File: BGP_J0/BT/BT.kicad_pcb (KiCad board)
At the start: 2 copper layers, 28 x 25 mm, 21 parts, among them P1 CONN_01X02, P2 CONN_01X02, P3 CONN_01X02, P4 CONN_01X04, P5 CONN_01X02, Q1 J202

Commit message: PCB Layout cleanup
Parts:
- moved RV1 5.10 mm to (158.2, 88.1), turned to 0 degrees
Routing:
- net Net-(C3-Pad1): track 13.7 -> 7.61 mm
- net Net-(Q1-Pad2): track 18.4 -> 22.5 mm
- net VCC: track 14.4 -> 12.8 mm
- net /Vref: track 0.00 -> 1.36 mm
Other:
- rule trace_min: 0.2 -> 0.3
- rule via_min_size: 0.4 -> 0.6
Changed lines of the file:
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@@
     (links 34)
     (no_connects 0)
-    (area 132.924999 78.924999 161.075001 104.075001)
+    (area 130.364286 78.924999 161.175001 105.75588)
     (thickness 1.6)
     (drawings 8)
-    (tracks 104)
+    (tracks 106)
     (zones 0)
     (modules 21)
@@
     (zone_clearance 0.3)
     (zone_45_only no)
-    (trace_min 0.2)
+    (trace_min 0.3)
     (segment_width 0.2)
     (edge_width 0.15)
     (via_size 0.6)
     (via_drill 0.4)
-    (via_min_size 0.4)
+    (via_min_size 0.6)
     (via_min_drill 0.3)
     (uvia_size 0.3)
     (uvia_drill 0.1)
     (uvias_allowed no)
-    (uvia_min_size 0.2)
+    (uvia_min_size 0.3)
     (uvia_min_drill 0.1)
     (pcb_text_width 0.3)
@@
   )
   (module Potentiometers:Potentiometer_Trimmer_Bourns_3296W (layer B.Cu)
-    (at 153.1 88.1 180)
+    (at 158.2 88.1)
     (descr "Spindle Trimmer Potentiometer, Bourns 3296W, https://www.bourns.com/pdfs/3296.pdf")
     (tags "Spindle Trimmer Potentiometer   Bourns 3296W")
-    (fp_text reference RV1 (at 1.56 3 180) (layer B.SilkS)
+    (fp_text reference RV1 (at 1.56 3) (layer B.SilkS)
       (effects (font (size 0.6 0.6) (thickness 0.15)) (justify mirror))
     )
-    (fp_text value POT (at -2.54 -3.67 180) (layer B.Fab) hide
+    (fp_text value POT (at -2.54 -3.67) (layer B.Fab) hide
       (effects (font (size 0.6 0.6) (thickness 0.15)) (justify mirror))
     )
@@
     (fp_line (start 2.5 -2.7) (end 2.5 2.7) (layer B.CrtYd) (width 0.05))
     (fp_line (start 2.5 2.7) (end -7.6 2.7) (layer B.CrtYd) (width 0.05))
-    (pad 1 thru_hole circle (at 0 0 180) (size 1.44 1.44) (drill 0.8) (layers *.Cu *.Mask)
+    (pad 1 thru_hole circle (at 0 0) (size 1.44 1.44) (drill 0.8) (layers *.Cu *.Mask)
       (net 16 "Net-(Q1-Pad2)"))
-    (pad 2 thru_hole circle (at -2.54 0 180) (size 1.44 1.44) (drill 0.8) (layers *.Cu *.Mask)
+    (pad 2 thru_hole circle (at -2.54 0) (size 1.44 1.44) (drill 0.8) (layers *.Cu *.Mask)
       (net 16 "Net-(Q1-Pad2)"))
-    (pad 3 thru_hole circle (at -5.08 0 180) (size 1.44 1.44) (drill 0.8) (layers *.Cu *.Mask)
+    (pad 3 thru_hole circle (at -5.08 0) (size 1.44 1.44) (drill 0.8) (layers *.Cu *.Mask)
       (net 4 "Net-(C3-Pad1)"))
     (model Potentiometers.3dshapes/Potentiometer_Trimmer_Bourns_3296W.wrl
@@
   (segment (start 141.5 99.10051) (end 143.80051 96.8) (width 0.3) (layer F.Cu) (net 2))
   (segment (start 146 96.4) (end 146 95.17602) (width 0.3) (layer F.Cu) (net 2))
+  (via (at 142.963596 91.736404) (size 0.6) (drill 0.4) (layers F.Cu B.Cu) (net 3))
+  (segment (start 143 92.9) (end 143 91.772808) (width 0.3) (layer F.Cu) (net 3))
+  (segment (start 143 91.772808) (end 142.963596 91.736404) (width 0.3) (layer F.Cu) (net 3))
   (segment (start 138.9 100.4) (end 138.9 101.4) (width 0.3) (layer F.Cu) (net 3))
   (segment (start 138.9 101.4) (end 139.8 102.3) (width 0.3) (layer F.Cu) (net 3))
@@
   (segment (start 152 94.95) (end 152 96.1) (width 0.3) (layer F.Cu) (net 3))
   (via (at 152 96.1) (size 0.6) (drill 0.4) (layers F.Cu B.Cu) (net 3))
-  (segment (start 143 92.9) (end 143 91.7) (width 0.3) (layer F.Cu) (net 3))
-  (via (at 143 91.7) (size 0.6) (drill 0.4) (layers F.Cu B.Cu) (net 3))
   (segment (start 146 86.82398) (end 146 85.5) (width 0.3) (layer F.Cu) (net 3))
   (via (at 146 85.5) (size 0.6) (drill 0.4) (layers F.Cu B.Cu) (net 3))
@@
   (segment (start 137 80.9) (end 136 80.9) (width 0.3) (layer F.Cu) (net 3))
   (via (at 136 80.9) (size 0.6) (drill 0.4) (layers F.Cu B.Cu) (net 3))
-  (segment (start 158.18 88.1) (end 156.88 86.8) (width 0.3) (layer F.Cu) (net 4))
-  (segment (start 156.88 86.8) (end 150.960002 86.8) (width 0.3) (layer F.Cu) (net 4))
-  (segment (start 150.960002 86.8) (end 149.710003 88.049999) (width 0.3) (layer F.Cu) (net 4))
-  (segment (start 149.710003 88.049999) (end 148.189999 88.049999) (width 0.3) (layer F.Cu) (net 4))
-  (segment (start 148.189999 88.049999) (end 148.139998 88.1) (width 0.3) (layer F.Cu) (net 4))
-  (segment (start 148.139998 88.1) (end 148.1 88.1) (width 0.3) (layer F.Cu) (net 4))
-  (segment (start 148.1 88.1) (end 147.02398 89.17602) (width 0.3) (layer F.Cu) (net 4))
-  (segment (start 147.02398 89.17602) (end 146 89.17602) (width 0.3) (layer F.Cu) (net 4))
+  (segment (start 153.12 88.1) (end 152.101767 88.1) (width 0.3) (layer F.Cu) (net 4))
+  (segment (start 152.101767 88.1) (end 152.051766 88.049999) (width 0.3) (layer F.Cu) (net 4))
+  (segment (start 147.20043 89.17602) (end 146 89.17602) (width 0.3) (layer F.Cu) (net 4))
+  (segment (start 152.051766 88.049999) (end 148.326451 88.049999) (width 0.3) (layer F.Cu) (net 4))
+  (segment (start 148.326451 88.049999) (end 147.20043 89.17602) (width 0.3) (layer F.Cu) (net 4))
   (segment (start 149 86.9) (end 149 86) (width 0.3) (layer F.Cu) (net 5))
   (segment (start 149 86) (end 149 83.1) (width 0.3) (layer F.Cu) (net 5))
@@
   (segment (start 140 90) (end 147.6 82.4) (width 0.3) (layer B.Cu) (net 12))
   (segment (start 147.6 82.4) (end 152.4 82.4) (width 0.3) (layer B.Cu) (net 12))
-  (segment (start 154.4 82.4) (end 154.4 83.8) (width 0.3) (layer F.Cu) (net 13))
-  (segment (start 154.4 83.8) (end 155.5 84.9) (width 0.3) (layer F.Cu) (net 13))
-  (segment (start 155.5 84.9) (end 158.2 84.9) (width 0.3) (layer F.Cu) (net 13))
-  (segment (start 158.2 84.9) (end 159.5 86.2) (width 0.3) (layer F.Cu) (net 13))
-  (segment (start 159.5 86.2) (end 159.5 91.1) (width 0.3) (layer F.Cu) (net 13))
+  (segment (start 154.4 82.4) (end 154.4 82.5) (width 0.3) (layer F.Cu) (net 13))
+  (segment (start 154.4 82.5) (end 159.5 87.6) (width 0.3) (layer F.Cu) (net 13))
+  (segment (start 159.5 87.6) (end 159.5 91.1) (width 0.3) (layer F.Cu) (net 13))
   (segment (start 159.5 91.1) (end 159 91.6) (width 0.3) (layer F.Cu) (net 13))
   (segment (start 159 91.6) (end 159 92.9) (width 0.3) (layer F.Cu) (net 13))
+  (segment (start 156.4 82.4) (end 156.4 83.55) (width 0.3) (layer F.Cu) (net 14))
+  (segment (start 156.4 83.55) (end 156.55 83.7) (width 0.3) (layer F.Cu) (net 14))
   (segment (start 156.6 94.95) (end 158.85 94.95) (width 0.3) (layer F.Cu) (net 15))
   (segment (start 158.85 94.95) (end 159 95.1) (width 0.3) (layer F.Cu) (net 15))
@@
   (segment (start 149 89.1) (end 149.2 89.3) (width 0.3) (layer F.Cu) (net 15))
   (segment (start 158.6 95.1) (end 159 95.1) (width 0.3) (layer F.Cu) (net 15))
-  (segment (start 156.6 93.05) (end 156.6 89.06) (width 0.3) (layer F.Cu) (net 16))
-  (segment (start 156.6 89.06) (end 155.64 88.1) (width 0.3) (layer F.Cu) (net 16))
-  (segment (start 144.3 88.1) (end 153.1 88.1) (width 0.3) (layer B.Cu) (net 16))
-  (segment (start 143 89.1) (end 143.3 89.1) (width 0.3) (layer F.Cu) (net 16))
-  (segment (start 143.3 89.1) (end 144.3 88.1) (width 0.3) (layer F.Cu) (net 16))
-  (via (at 144.3 88.1) (size 0.6) (drill 0.4) (layers F.Cu B.Cu) (net 16))
-  (segment (start 155.64 88.1) (end 153.1 88.1) (width 0.3) (layer F.Cu) (net 16))
+  (segment (start 143 90) (end 143.3 90.3) (width 0.3) (layer F.Cu) (net 16))
+  (segment (start 143.3 90.3) (end 143.4 90.3) (width 0.3) (layer F.Cu) (net 16))
+  (segment (start 143 89.1) (end 143 90) (width 0.3) (layer F.Cu) (net 16))
+  (segment (start 143.824264 90.3) (end 143.4 90.3) (width 0.3) (layer B.Cu) (net 16))
+  (segment (start 153.46 90.3) (end 143.824264 90.3) (width 0.3) (layer B.Cu) (net 16))
+  (segment (start 155.66 88.1) (end 153.46 90.3) (width 0.3) (layer B.Cu) (net 16))
+  (via (at 143.4 90.3) (size 0.6) (drill 0.4) (layers F.Cu B.Cu) (net 16))
+  (segment (start 155.66 88.1) (end 155.66 92.16) (width 0.3) (layer F.Cu) (net 16))
+  (segment (start 155.66 92.16) (end 156.55 93.05) (width 0.3) (layer F.Cu) (net 16))
+  (segment (start 156.55 93.05) (end 156.6 93.05) (width 0.3) (layer F.Cu) (net 16))
+  (segment (start 158.2 88.1) (end 155.66 88.1) (width 0.3) (layer F.Cu) (net 16))
   (zone (net 14) (net_name /Vref) (layer F.Cu) (hatch edge 0.508)
     (connect_pads (clearance 0.3))

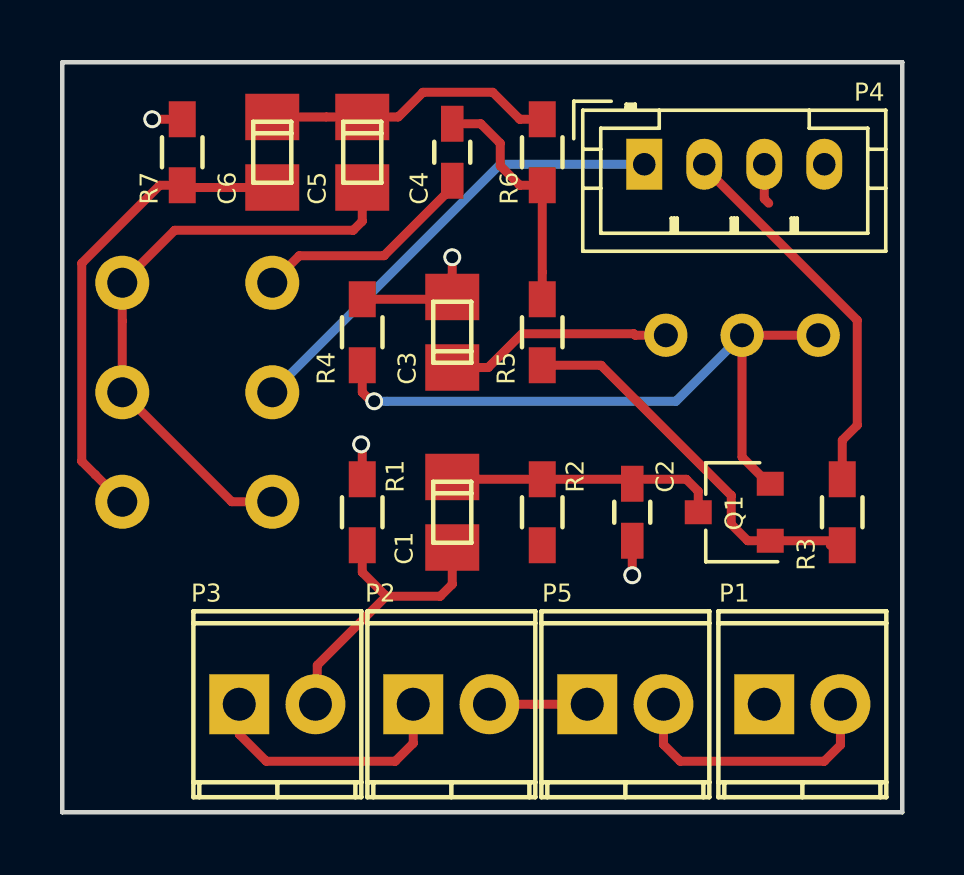
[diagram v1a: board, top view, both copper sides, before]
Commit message: Changed Term Blocks in BT stack to JST connector to BND
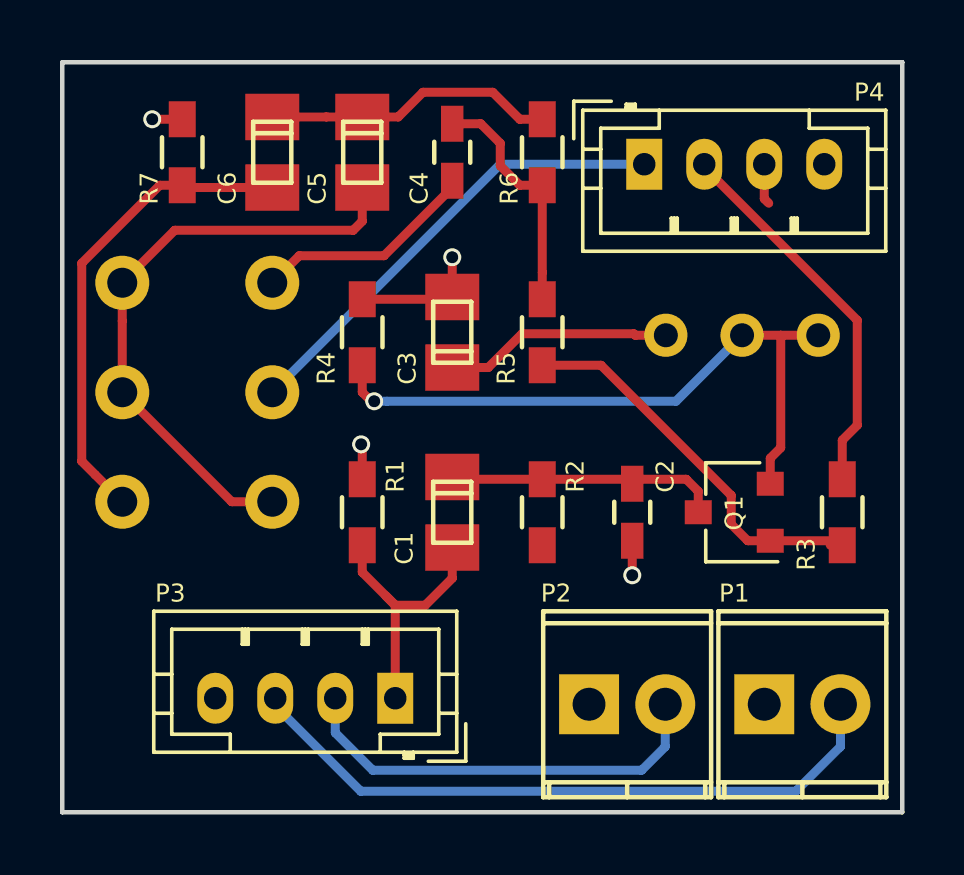
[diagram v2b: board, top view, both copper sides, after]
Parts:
- removed P5: CONN_01X02, Terminal_Blocks:TerminalBlock_Pheonix_MPT-2.54mm_2pol
- P3: value CONN_01X02 -> CONN_01X04; footprint Terminal_Blocks:TerminalBlock_Pheonix_MPT-2.54mm_2pol -> Connectors_JST:JST_PH_B4B-PH-K_04x2.00mm_Straight
- moved P2 5.86 mm to (150.6, 100.4)
- moved P3 5.20 mm to (144.1, 100.2), turned to 180 degrees
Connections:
- P3 pad 1: Earth -> /IN
- P3 pad 2: /IN -> /IN_N
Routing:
- net /IN_B: track 9.06 -> 22.3 mm
- net /IN_N: track 3.26 -> 14.4 mm
- net Earth: track 16.4 -> 7.68 mm
- net /IN: track 10.2 -> 9.28 mm

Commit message: Flipped BT to VOL connector on BT board to bottom side for better conn
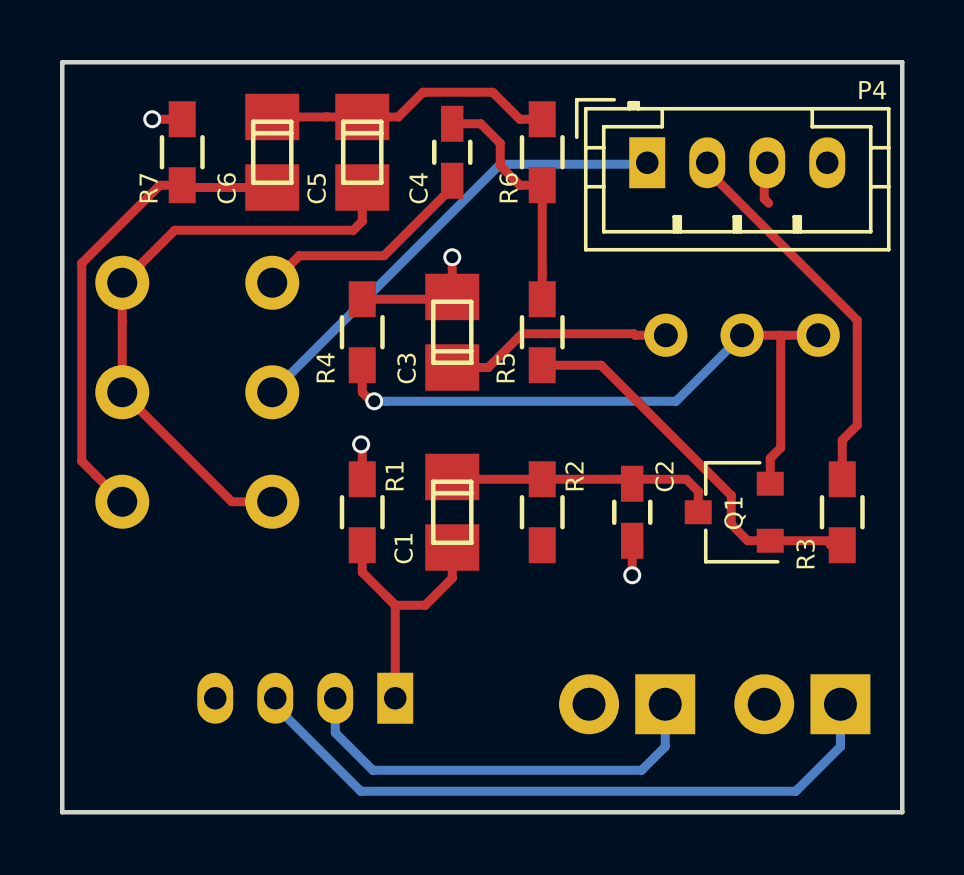
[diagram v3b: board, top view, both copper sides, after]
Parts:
- P1, P2, P3: moved to B.Cu
- moved P1 2.54 mm to (158.9, 100.4), turned to 180 degrees
- moved P2 2.54 mm to (153.1, 100.4), turned to 180 degrees
- moved P4 0.11 mm to (152.5, 82.3)
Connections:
- P1 pad 1: Earth -> /IN_B
- P1 pad 2: /IN_B -> Earth
- P2 pad 1: Earth -> /IN_N
- P2 pad 2: /IN_N -> Earth

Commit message: Changed POT, parallel VOL pot conn for offboard pot
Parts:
- Q1: value J202 -> MMBF5457
- R3: value 12k -> 10k
- R4: value 6.8k -> 4.99k
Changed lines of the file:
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@@
-(kicad_pcb (version 4) (host pcbnew 4.0.7)
+(kicad_pcb (version 4) (host pcbnew 4.0.4-1.fc24-product)
   (general
     (links 34)
@@
       (effects (font (size 0.6 0.6) (thickness 0.15)))
     )
-    (fp_text value J202 (at 0 2.5 180) (layer F.Fab) hide
+    (fp_text value MMBF5457 (at 0 2.5 180) (layer F.Fab) hide
       (effects (font (size 0.6 0.6) (thickness 0.15)))
     )
@@
       (effects (font (size 0.6 0.6) (thickness 0.15)))
     )
-    (fp_text value 12k (at 0 1.9 270) (layer F.Fab) hide
+    (fp_text value 10k (at 0 1.9 270) (layer F.Fab) hide
       (effects (font (size 0.6 0.6) (thickness 0.15)))
     )
@@
       (effects (font (size 0.6 0.6) (thickness 0.15)))
     )
-    (fp_text value 6.8k (at 0 1.9 90) (layer F.Fab) hide
-      (effects (font (size 0.6 0.6) (thickness 0.15)))
-    )
+    (fp_text value 4.99k (at 0 1.9 90) (layer F.Fab) hide
+      (effects (font (size 0.6 0.6) (thickness 0.15)))
+    )

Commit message: Some cleanup, and gain stage changes
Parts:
- R3: value 10k -> 12k
- R4: value 4.99k -> 6.8k
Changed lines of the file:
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@@
       (effects (font (size 0.6 0.6) (thickness 0.15)))
     )
-    (fp_text value 10k (at 0 1.9 270) (layer F.Fab) hide
+    (fp_text value 12k (at 0 1.9 270) (layer F.Fab) hide
       (effects (font (size 0.6 0.6) (thickness 0.15)))
     )
@@
       (effects (font (size 0.6 0.6) (thickness 0.15)))
     )
-    (fp_text value 4.99k (at 0 1.9 90) (layer F.Fab) hide
+    (fp_text value 6.8k (at 0 1.9 90) (layer F.Fab) hide
       (effects (font (size 0.6 0.6) (thickness 0.15)))
     )
